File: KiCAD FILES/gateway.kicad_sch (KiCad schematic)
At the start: 167 parts, among them J1 Conn_01x02_Pin, J10 SIM7100-8-1-15-00-A_REVC, J12 Conn_01x02_Pin, J13 Conn_01x02_Pin, J14 B2B-XH-A_LF__SN_, J15 B2B-XH-A_LF__SN_, J16 B4B-XH-A_LF__SN_, J17 B4B-XH-A_LF__SN_, J18 B4B-XH-A_LF__SN_, J19 MEM2067-02-180-00-A_REVB, J2 Conn_01x02_Pin, J20 B3B-XH-A_LF__SN_, J21 B3B-XH-A_LF__SN_, J24 B2B-XH-A_LF__SN_, J28 B4B-XH-A_LF__SN_, J29 B2B-XH-A_LF__SN_, J31 TYPE-C-31-M-12, J32 B3B-XH-A_LF__SN_, J35 Conn_01x02_Pin, J37 B3B-XH-A_LF__SN_, J38 Conn_01x02_Pin, J39 Conn_01x02_Pin, J40 Conn_01x06_Pin, J9 Conn_01x04_Pin, Q1 MMBT3904, Q2 MMBT3904, Q3 MMBT3904, U1 TXB0108RGYR, U11 AMS1117-3.3, U14 AMS1117-3.3, U16 AMS1117-3.3, U18 AMS1117-3.3, U2 ESP32-WROOM-32E__4MB_HIGH_TEM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, U3 SIM7000E, U4 MPL3115A2, U6 DS3231MZ_TRL, U7 Ai-Thinker RA-08H, U8 ST3485EBDR, U9 FT232RL-REEL

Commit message: RESTRUCTURING FILES
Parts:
- removed J16: B4B-XH-A_LF__SN_, B4B-XH-A_LF__SN_:JST_B4B-XH-A_LF__SN_, symbol B4B-XH-A_LF__SN_:B4B-XH-A_LF__SN_
- added J3: B3B-XH-A_LF__SN_, B3B-XH-A_LF__SN_:JST_B3B-XH-A_LF__SN_, symbol B3B-XH-A_LF__SN_:B3B-XH-A_LF__SN_
- added R38, R54, R55, R61: 4.7k, Resistor_SMD:R_0603_1608Metric, symbol Device:R
- added R62: 10K, Resistor_SMD:R_0603_1608Metric, symbol Device:R
- added R63: 20K, Resistor_SMD:R_0603_1608Metric, symbol Device:R
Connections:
- net 3v3: now also R55.2, R61.2
- net DAVIS 7852: now also J40.4 (Pin_4), U2.10 (IO25), J3.1, R61.1; no longer J40.1 (Pin_1), U2.6 (IO34)
- net ESP32 power in: now also R38.2, R54.2
- net GND: now also J3.2, J3.3, R63.1
- net I2C SCL: now also R54.1
- net I2C SDA: now also R38.1
- net INSPEED VORTEX: now also R55.1
- net INSPEEED VANE: now also R62.2, R63.2; no longer J37.2
- net VH400: now also J40.1 (Pin_1), U2.6 (IO34); no longer J40.4 (Pin_4), U2.10 (IO25)
- new net: J37.2, R62.1
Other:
- moved on the sheet: C38, C39, C40, C41, C42, C76, C78, D17, D18, D20, D21, J14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

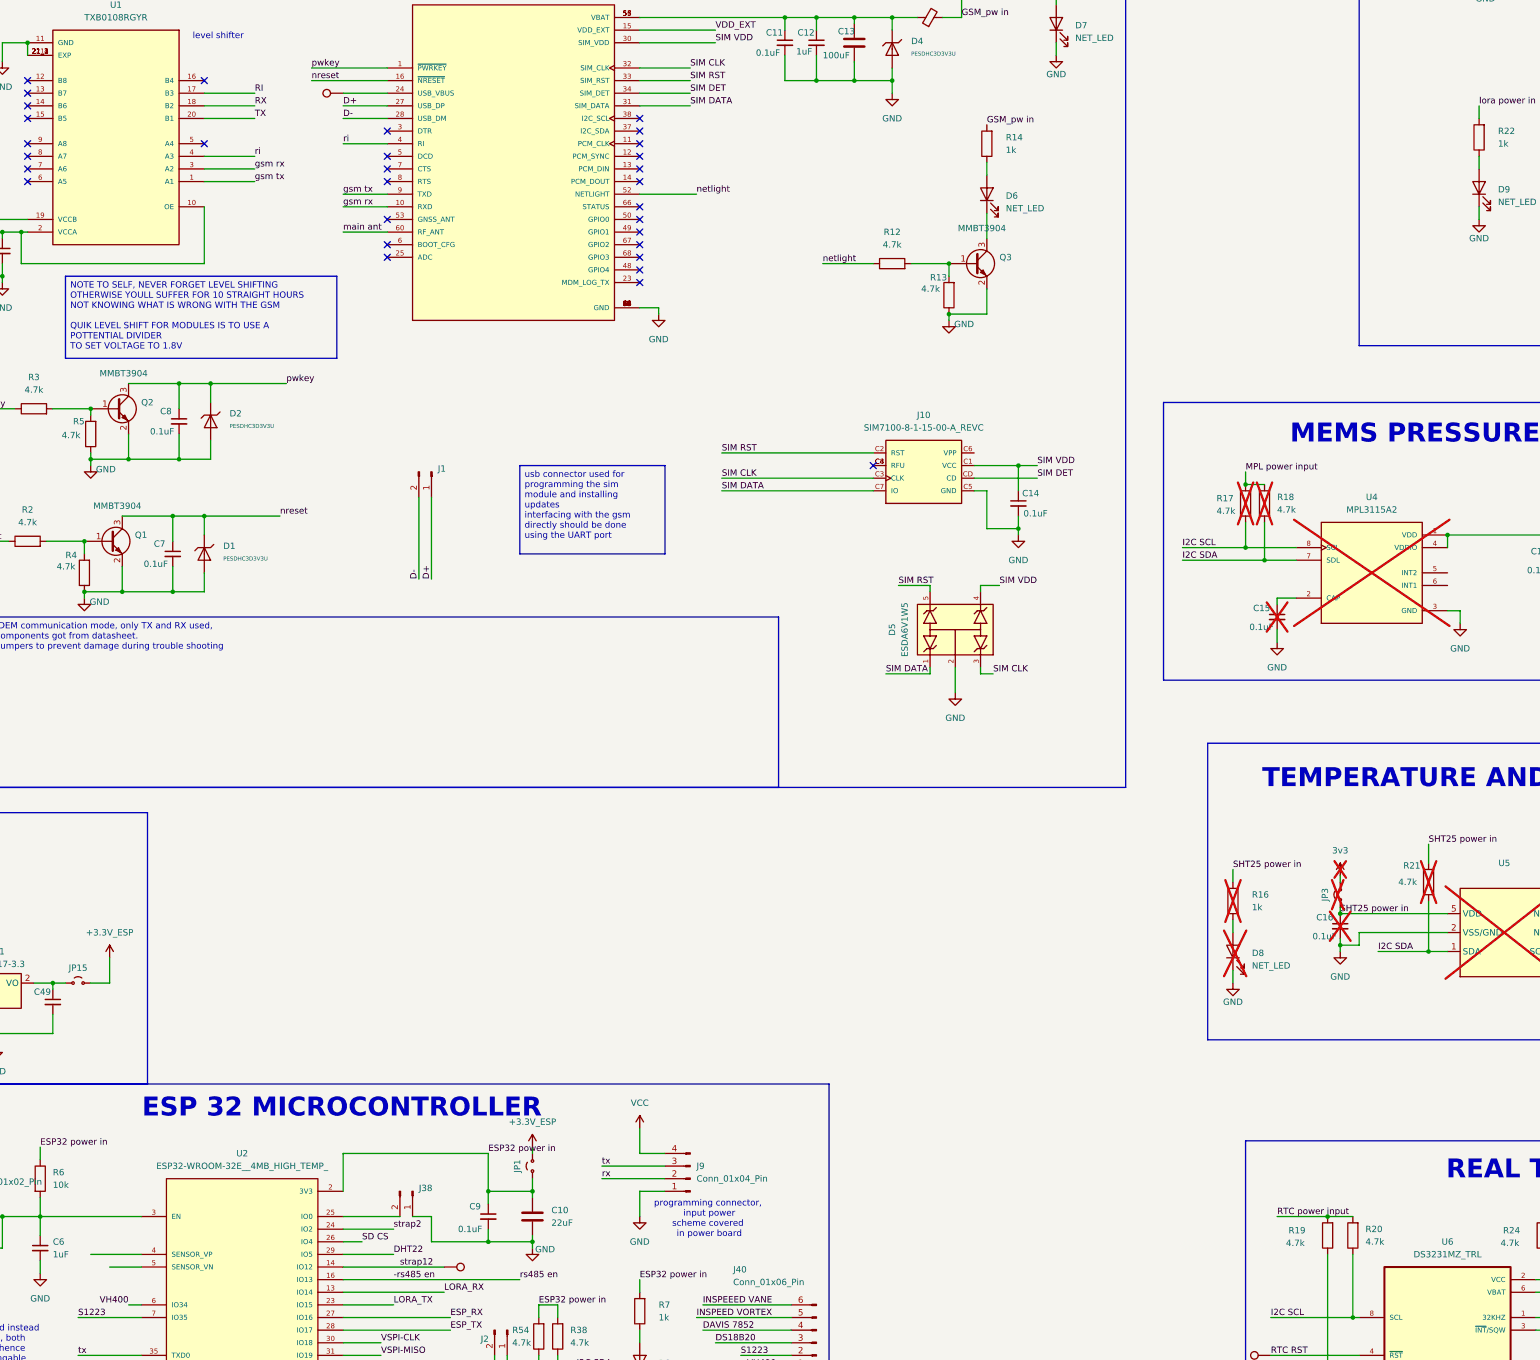
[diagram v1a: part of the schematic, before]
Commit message: updates to gsm code, connected to things speak,
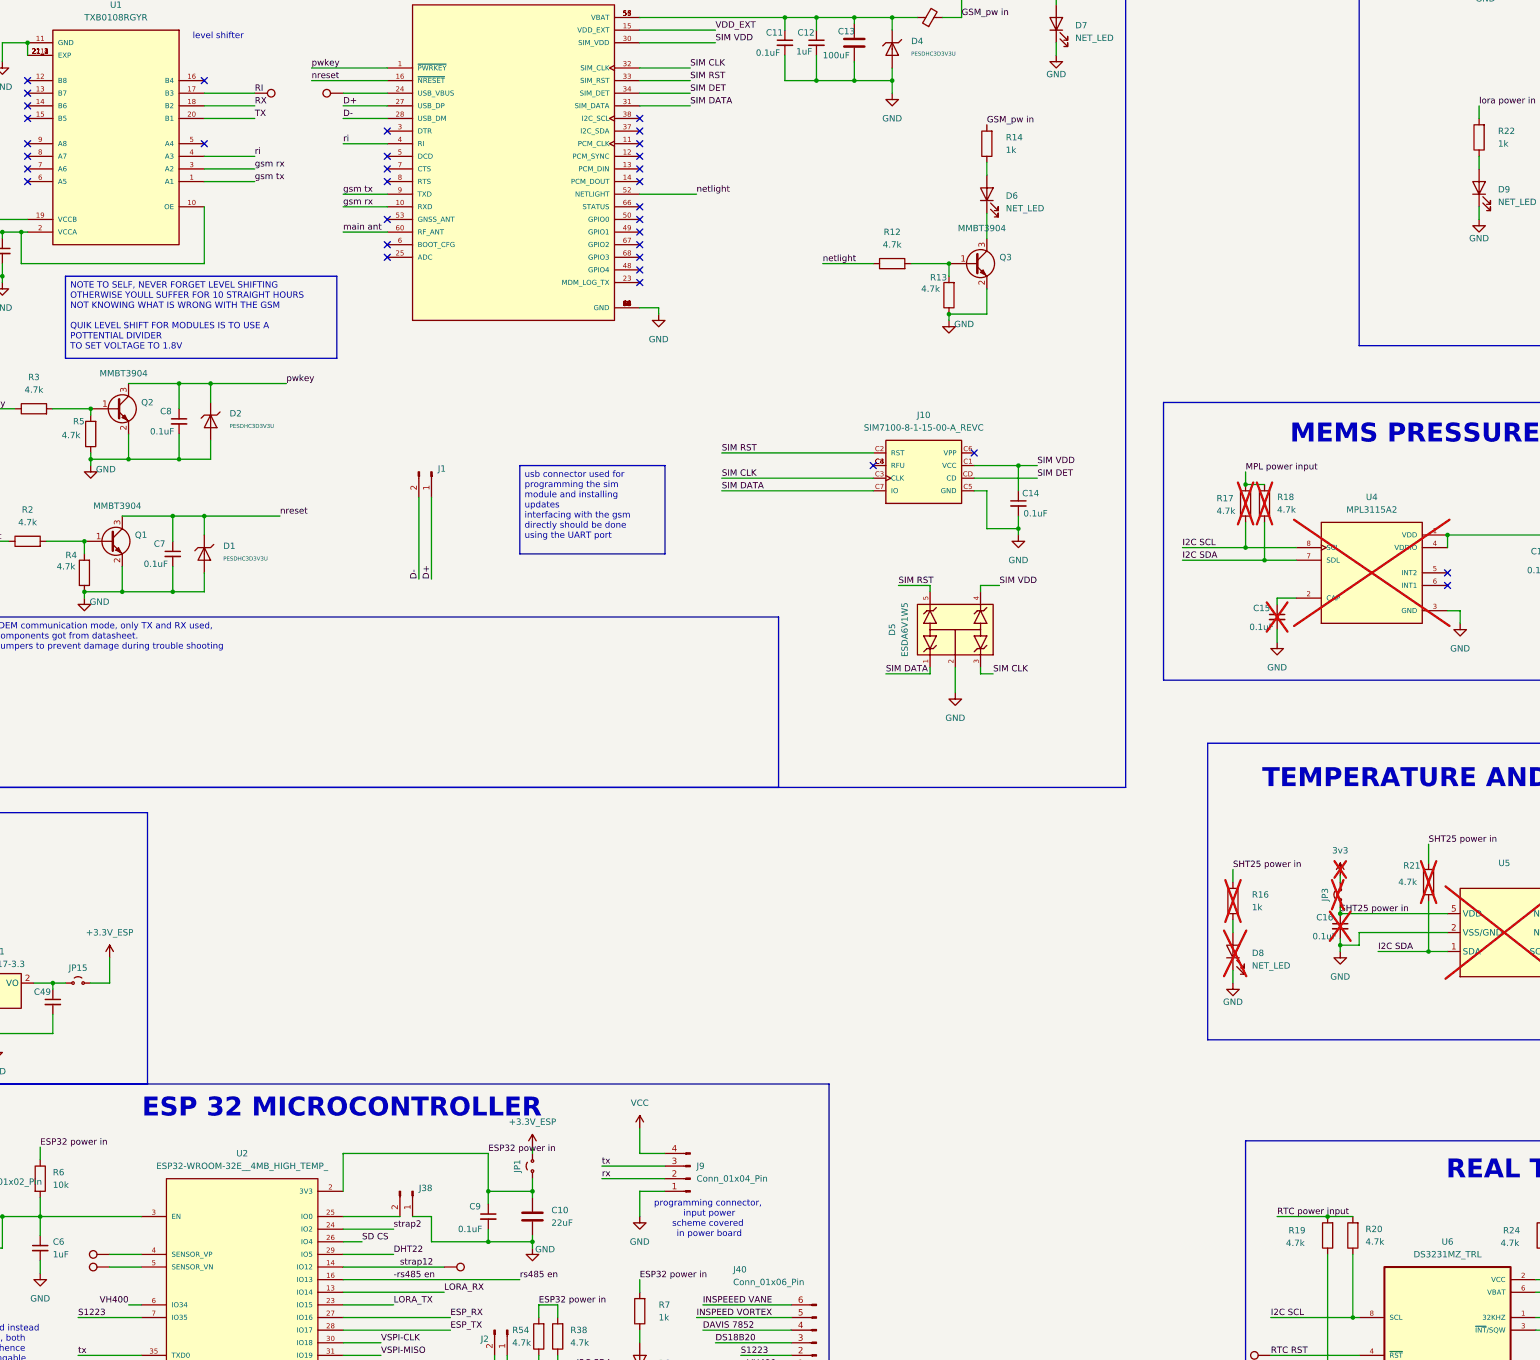
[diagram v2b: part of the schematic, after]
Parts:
- added SNS_TX16, SNS_TX17, SNS_TX18: TestPoint, TestPoint:TestPoint_Pad_D1.5mm, symbol Connector:TestPoint
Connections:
- net RI: now also SNS_TX18.1
- net at U2.4 (SENSOR_VP): now also SNS_TX16.1
- net at U2.5 (SENSOR_VN): now also SNS_TX17.1
- no-connect marks 48 -> 51
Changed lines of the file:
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@@
 	)
 	(no_connect
+		(at 351.79 231.14)
+	)
+	(no_connect
 		(at 513.08 218.44)
 	)
@@
 	)
 	(no_connect
+		(at 256.54 204.47)
+	)
+	(no_connect
 		(at 189.23 139.7)
 	)
@@
 	)
 	(no_connect
+		(at 351.79 228.6)
+	)
+	(no_connect
 		(at 66.04 149.86)
 	)
@@
 	(wire
 		(pts
-			(xy 78.74 365.76) (xy 88.9 365.76)
+			(xy 82.55 365.76) (xy 88.9 365.76)
 		)
 		(stroke
@@
 	)
 	(symbol
+		(lib_id "Connector:TestPoint")
+		(at 111.76 132.08 270)
+		(unit 1)
+		(exclude_from_sim no)
+		(in_bom no)
+		(on_board yes)
+		(dnp no)
+		(property "Reference" "SNS_TX18"
+			(at 125.476 131.826 90)
+			(effects
+				(font
+					(size 1.27 1.27)
+				)
+				(justify right)
+				(hide yes)
+			)
+		)
+		(property "Value" "TestPoint"
+			(at 113.7921 134.62 0)
+			(effects
+				(font
+					(size 1.27 1.27)
+				)
+				(justify left)
+				(hide yes)
+			)
+		)
+		(property "Footprint" "TestPoint:TestPoint_Pad_D1.5mm"
+			(at 111.76 137.16 0)
+			(effects
+				(font
+					(size 1.27 1.27)
+				)
+				(hide yes)
+			)
+		)
+		(property "Datasheet" "~"
+			(at 111.76 137.16 0)
+			(effects
+				(font
+					(size 1.27 1.27)
+				)
+				(hide yes)
+			)
+		)
+		(property "Description" "test point"
+			(at 111.76 132.08 0)
+			(effects
+				(font
+					(size 1.27 1.27)
+				)
+				(hide yes)
+			)
+		)
+		(pin "1"
+		)
+		(instances
+			(project "AWS PROJECT"
+				(path "/28dd5718-f0db-4cd1-9b2d-c2f5533a75a3/918a84d0-2382-4e9e-a083-abfab5a808df"
+					(reference "SNS_TX18")
+					(unit 1)
+				)
+			)
+		)
+	)
+	(symbol
 		(lib_id "Device:C_Small")
 		(at 397.51 374.65 0)
@@
 	)
 	(symbol
+		(lib_id "Connector:TestPoint")
+		(at 82.55 365.76 90)
+		(unit 1)
+		(exclude_from_sim no)
+		(in_bom no)
+		(on_board yes)
+		(dnp no)
+		(property "Reference" "SNS_TX16"
+			(at 68.834 366.014 90)
+			(effects
+				(font
+					(size 1.27 1.27)
+				)
+				(justify right)
+				(hide yes)
+			)
+		)
+		(property "Value" "TestPoint"
+			(at 80.5179 363.22 0)
+			(effects
+				(font
+					(size 1.27 1.27)
+				)
+				(justify left)
+				(hide yes)
+			)
+		)
+		(property "Footprint" "TestPoint:TestPoint_Pad_D1.5mm"
+			(at 82.55 360.68 0)
+			(effects
+				(font
+					(size 1.27 1.27)
+				)
+				(hide yes)
+			)
+		)
+		(property "Datasheet" "~"
+			(at 82.55 360.68 0)
+			(effects
+				(font
+					(size 1.27 1.27)
+				)
+				(hide yes)
+			)
+		)
+		(property "Description" "test point"
+			(at 82.55 365.76 0)
+			(effects
+				(font
+					(size 1.27 1.27)
+				)
+				(hide yes)
+			)
+		)
+		(pin "1"
+		)
+		(instances
+			(project "AWS PROJECT"
+				(path "/28dd5718-f0db-4cd1-9b2d-c2f5533a75a3/918a84d0-2382-4e9e-a083-abfab5a808df"
+					(reference "SNS_TX16")
+					(unit 1)
+				)
+			)
+		)
+	)
+	(symbol
 		(lib_id "power:GND")
 		(at 496.57 444.5 0)
@@
 					(unit 1)
 				)
+			)
+		)
+	)
+	(symbol
+		(lib_id "Connector:TestPoint")
+		(at 82.55 368.3 90)
+		(unit 1)
+		(exclude_from_sim no)
+		(in_bom no)
+		(on_board yes)
+		(dnp no)
+		(property "Reference" "SNS_TX17"
+			(at 68.834 368.554 90)
+			(effects
+				(font
+					(size 1.27 1.27)
+				)
+				(justify right)
+				(hide yes)
+			)
+		)
+		(property "Value" "TestPoint"
+			(at 80.5179 365.76 0)
+			(effects
+				(font
+					(size 1.27 1.27)
+				)
+				(justify left)
+				(hide yes)
+			)
+		)
+		(property "Footprint" "TestPoint:TestPoint_Pad_D1.5mm"
+			(at 82.55 363.22 0)
+			(effects
+				(font
+					(size 1.27 1.27)
+				)
+				(hide yes)
+			)
+		)
+		(property "Datasheet" "~"
+			(at 82.55 363.22 0)
+			(effects
+				(font
+					(size 1.27 1.27)
+				)
+				(hide yes)
+			)
+		)
+		(property "Description" "test point"
+			(at 82.55 368.3 0)
+			(effects
+				(font
+					(size 1.27 1.27)
+				)
+				(hide yes)
+			)
+		)
+		(pin "1"
+		)
+		(instances
+			(project "AWS PROJECT"
+				(path "/28dd5718-f0db-4cd1-9b2d-c2f5533a75a3/918a84d0-2382-4e9e-a083-abfab5a808df"
+					(reference "SNS_TX17")
+					(unit 1)
+				)

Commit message: changes to pcb and 3d mdel
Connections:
- net VCC is gone; now on net 5v: D20.2 (A), J9.4 (Pin_4), JP16.2 (B), R50.2, R51.2
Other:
- moved on the sheet: J18
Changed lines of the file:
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@@
 	)
 	(junction
-		(at 480.06 375.92)
+		(at 500.38 369.57)
+		(diameter 0)
+		(color 0 0 0 0)
+	)
+	(junction
+		(at 500.38 377.19)
 		(diameter 0)
 		(color 0 0 0 0)
@@
 	(wire
 		(pts
-			(xy 483.87 370.84) (xy 480.06 370.84)
+			(xy 504.19 372.11) (xy 500.38 372.11)
 		)
 		(stroke
@@
 	(wire
 		(pts
-			(xy 480.06 370.84) (xy 480.06 375.92)
+			(xy 500.38 372.11) (xy 500.38 377.19)
 		)
 		(stroke
@@
 	(wire
 		(pts
-			(xy 476.25 368.3) (xy 483.87 368.3)
+			(xy 496.57 369.57) (xy 500.38 369.57)
 		)
 		(stroke
@@
 	(wire
 		(pts
-			(xy 472.44 373.38) (xy 483.87 373.38)
+			(xy 492.76 374.65) (xy 504.19 374.65)
 		)
 		(stroke
@@
 	(wire
 		(pts
-			(xy 480.06 375.92) (xy 483.87 375.92)
+			(xy 500.38 377.19) (xy 504.19 377.19)
 		)
 		(stroke
@@
 	(wire
 		(pts
+			(xy 500.38 359.41) (xy 500.38 369.57)
+		)
+		(stroke
+			(width 0)
+			(type default)
+		)
+	)
+	(wire
+		(pts
 			(xy 96.52 195.58) (xy 96.52 190.5)
 		)
@@
 	(wire
 		(pts
+			(xy 500.38 369.57) (xy 504.19 369.57)
+		)
+		(stroke
+			(width 0)
+			(type default)
+		)
+	)
+	(wire
+		(pts
 			(xy 317.5 233.68) (xy 317.5 234.95)
 		)
@@
 	(wire
 		(pts
-			(xy 480.06 375.92) (xy 480.06 379.73)
+			(xy 500.38 377.19) (xy 500.38 381)
 		)
 		(stroke
@@
 	)
 	(symbol
+		(lib_id "power:VCC")
+		(at 500.38 359.41 0)
+		(unit 1)
+		(exclude_from_sim no)
+		(in_bom yes)
+		(on_board yes)
+		(dnp no)
+		(fields_autoplaced yes)
+		(property "Reference" "#PWR0151"
+			(at 500.38 363.22 0)
+			(effects
+				(font
+					(size 1.27 1.27)
+				)
+				(hide yes)
+			)
+		)
+		(property "Value" "VCC"
+			(at 500.38 354.33 0)
+			(effects
+				(font
+					(size 1.27 1.27)
+				)
+			)
+		)
+		(property "Footprint" ""
+			(at 500.38 359.41 0)
+			(effects
+				(font
+					(size 1.27 1.27)
+				)
+				(hide yes)
+			)
+		)
+		(property "Datasheet" ""
+			(at 500.38 359.41 0)
+			(effects
+				(font
+					(size 1.27 1.27)
+				)
+				(hide yes)
+			)
+		)
+		(property "Description" "Power symbol creates a global label with name \"VCC\""
+			(at 500.38 359.41 0)
+			(effects
+				(font
+					(size 1.27 1.27)
+				)
+				(hide yes)
+			)
+		)
+		(pin "1"
+		)
+		(instances
+			(project "AWS PROJECT"
+				(path "/28dd5718-f0db-4cd1-9b2d-c2f5533a75a3/918a84d0-2382-4e9e-a083-abfab5a808df"
+					(reference "#PWR0151")
+					(unit 1)
+				)
+			)
+		)
+	)
+	(symbol
 		(lib_id "Device:C_Small")
 		(at 679.45 190.5 0)
@@
 	(symbol
 		(lib_id "power:VCC")
-		(at 476.25 368.3 0)
+		(at 496.57 369.57 0)
 		(unit 1)
 		(exclude_from_sim no)
@@
 		(fields_autoplaced yes)
 		(property "Reference" "#PWR0111"
-			(at 476.25 372.11 0)
+			(at 496.57 373.38 0)
 			(effects
 				(font
@@
 		)
 		(property "Value" "5v"
-			(at 476.25 363.22 0)
+			(at 496.57 364.49 0)
 			(effects
 				(font
@@
 		)
 		(property "Footprint" ""
-			(at 476.25 368.3 0)
+			(at 496.57 369.57 0)
 			(effects
 				(font
@@
 		)
 		(property "Datasheet" ""
-			(at 476.25 368.3 0)
+			(at 496.57 369.57 0)
 			(effects
 				(font
@@
 		)
 		(property "Description" "Power symbol creates a global label with name \"VCC\""
-			(at 476.25 368.3 0)
+			(at 496.57 369.57 0)
 			(effects
 				(font
@@
 	(symbol
 		(lib_id "power:VCC")
-		(at 472.44 373.38 0)
+		(at 492.76 374.65 0)
 		(unit 1)
 		(exclude_from_sim no)
@@
 		(fields_autoplaced yes)
 		(property "Reference" "#PWR081"
-			(at 472.44 377.19 0)
+			(at 492.76 378.46 0)
 			(effects
 				(font
@@
 		)
 		(property "Value" "3v3"
-			(at 472.44 368.3 0)
+			(at 492.76 369.57 0)
 			(effects
 				(font
@@
 		)
 		(property "Footprint" ""
-			(at 472.44 373.38 0)
+			(at 492.76 374.65 0)
 			(effects
 				(font
@@
 		)
 		(property "Datasheet" ""
-			(at 472.44 373.38 0)
+			(at 492.76 374.65 0)
 			(effects
 				(font
@@
 		)
 		(property "Description" "Power symbol creates a global label with name \"VCC\""
-			(at 472.44 373.38 0)
+			(at 492.76 374.65 0)
 			(effects
 				(font
@@
 	(symbol
 		(lib_id "power:GND")
-		(at 480.06 379.73 0)
+		(at 500.38 381 0)
 		(unit 1)
 		(exclude_from_sim no)
@@
 		(fields_autoplaced yes)
 		(property "Reference" "#PWR0113"
-			(at 480.06 386.08 0)
+			(at 500.38 387.35 0)
 			(effects
 				(font
@@
 		)
 		(property "Value" "GND"
-			(at 480.06 384.81 0)
+			(at 500.38 386.08 0)
 			(effects
 				(font
@@
 		)
 		(property "Footprint" ""
-			(at 480.06 379.73 0)
+			(at 500.38 381 0)
 			(effects
 				(font
@@
 		)
 		(property "Datasheet" ""
-			(at 480.06 379.73 0)
+			(at 500.38 381 0)
 			(effects
 				(font
@@
 		)
 		(property "Description" "Power symbol creates a global label with name \"GND\" , ground"
-			(at 480.06 379.73 0)
+			(at 500.38 381 0)
 			(effects
 				(font
@@
 	(symbol
 		(lib_id "B4B-XH-A_LF__SN_:B4B-XH-A_LF__SN_")
-		(at 491.49 370.84 0)
+		(at 511.81 372.11 0)
 		(unit 1)
 		(exclude_from_sim no)
@@
 		(fields_autoplaced yes)
 		(property "Reference" "J18"
-			(at 496.57 370.8399 0)
+			(at 516.89 372.1099 0)
 			(effects
 				(font
@@
 		)
 		(property "Value" "B4B-XH-A_LF__SN_"
-			(at 496.57 373.3799 0)
+			(at 516.89 374.6499 0)
 			(effects
 				(font
@@
 		)
 		(property "Footprint" "B4B-XH-A_LF__SN_:JST_B4B-XH-A_LF__SN_"
-			(at 491.49 370.84 0)
+			(at 511.81 372.11 0)
 			(effects
 				(font
@@
 		)
 		(property "Datasheet" ""
-			(at 491.49 370.84 0)
+			(at 511.81 372.11 0)
 			(effects
 				(font
@@
 		)
 		(property "Description" ""
-			(at 491.49 370.84 0)
+			(at 511.81 372.11 0)
 			(effects
 				(font
@@
 		)
 		(property "MF" "JST Sales"
-			(at 491.49 370.84 0)
+			(at 511.81 372.11 0)
 			(effects
 				(font
@@
 		)
 		(property "MAXIMUM_PACKAGE_HEIGHT" "7.00 mm"
-			(at 491.49 370.84 0)
+			(at 511.81 372.11 0)
 			(effects
 				(font
@@
 		)
 		(property "Package" "None"
-			(at 491.49 370.84 0)
+			(at 511.81 372.11 0)
 			(effects
 				(font
@@
 		)
 		(property "Price" "None"
-			(at 491.49 370.84 0)
+			(at 511.81 372.11 0)
 			(effects
 				(font
@@
 		)
 		(property "Check_prices" "https://www.snapeda.com/parts/B4B-XH-A(LF)(SN)/JST/view-part/?ref=eda"
-			(at 491.49 370.84 0)
+			(at 511.81 372.11 0)
 			(effects
 				(font
@@
 		)
 		(property "STANDARD" "Manufacturer Recommendations"
-			(at 491.49 370.84 0)
+			(at 511.81 372.11 0)
 			(effects
 				(font
@@
 		)
 		(property "PARTREV" "7/4/21"
-			(at 491.49 370.84 0)
+			(at 511.81 372.11 0)
 			(effects
 				(font
@@
 		)
 		(property "SnapEDA_Link" "https://www.snapeda.com/parts/B4B-XH-A(LF)(SN)/JST/view-part/?ref=snap"
-			(at 491.49 370.84 0)
+			(at 511.81 372.11 0)
 			(effects
 				(font
@@
 		)
 		(property "MP" "B4B-XH-A(LF)(SN)"
-			(at 491.49 370.84 0)
+			(at 511.81 372.11 0)
 			(effects
 				(font
@@
 		)
 		(property "Description_1" "Connector Header Through Hole 4 position 0.098 (2.50mm)"
-			(at 491.49 370.84 0)
+			(at 511.81 372.11 0)
 			(effects
 				(font
@@
 		)
 		(property "Availability" "In Stock"
-			(at 491.49 370.84 0)
+			(at 511.81 372.11 0)
 			(effects
 				(font
@@
 		)
 		(property "MANUFACTURER" "JST"
-			(at 491.49 370.84 0)
+			(at 511.81 372.11 0)
 			(effects
 				(font
